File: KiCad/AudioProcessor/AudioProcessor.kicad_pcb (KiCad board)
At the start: 2 copper layers, 56 x 43 mm, 49 parts, among them J1 IN4, J2 IN3, J3 IN2, J4 IN1, J5 AUX, J6 I2C, J7 LOUT, J8 ROUT, J9 POWER, U1 TDA7440

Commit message: Audio processor PCB is ready
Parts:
- removed R4, R5, R6, R7, R8: 600, Resistors_SMD:R_0603
- removed the REF** at (134.0, 71.3)
- removed the REF** at (101.1, 72.1)
- removed the REF** at (101.1, 67.7)
- removed the REF** at (101.0, 63.2)
- removed the REF** at (101.0, 58.6)
- removed the REF** at (118.2, 54.6)
- removed the REF** at (142.6, 90.5)
- removed the REF** at (100.9, 90.6)
- removed the REF** at (135.2, 83.7)
- removed the REF** at (131.2, 83.7)
- removed the REF** at (125.1, 88.1)
- removed the REF** at (121.2, 88.1)
- removed the REF** at (117.4, 88.1)
- removed the REF** at (113.7, 88.1)
- removed the REF** at (105.8, 82.6)
- removed the REF** at (105.8, 78.4)
- added C14: 2uf, Capacitors_SMD:C_0603, F.Cu at (119.5, 86.5)
- added C15: 2uf, Capacitors_SMD:C_0603, F.Cu at (119.5, 89.1)
- added C16: 2uf, Capacitors_SMD:C_0603, F.Cu at (119.5, 91.7)
- added C17: 2uf, Capacitors_SMD:C_0603, F.Cu at (119.5, 94.3)
- added C18: 2uf, Capacitors_SMD:C_0603, F.Cu at (116.2, 87.8)
- added C19: 2uf, Capacitors_SMD:C_0603, F.Cu at (116.2, 90.4)
- added C20: 2uf, Capacitors_SMD:C_0603, F.Cu at (116.3, 93.0)
- added C21: 2uf, Capacitors_SMD:C_0603, F.Cu at (116.3, 95.6)
- added C22: 100uf, Capacitors_THT:CP_Radial_Tantal_D6.0mm_P5.00mm, F.Cu at (141.0, 92.8)
- added C23: 4.7n, Capacitors_THT:C_Rect_L7.0mm_W2.0mm_P5.00mm, F.Cu at (142.1, 105.9)
- added C24: 1n, Capacitors_THT:C_Rect_L7.0mm_W2.0mm_P5.00mm, F.Cu at (142.1, 109.1)
- added J10: DPOT_10K, KiCadCustomLibs:Conn_1x03_2.54mm, F.Cu at (99.6, 89.4)
- added REF**: MountingHole_3mm, Mounting_Holes:MountingHole_3mm, F.Cu at (148.0, 112.0)
- added REF**: MountingHole_3mm, Mounting_Holes:MountingHole_3mm, F.Cu at (100.0, 112.0)
- added REF**: MountingHole_3mm, Mounting_Holes:MountingHole_3mm, F.Cu at (100.0, 83.0)
- added REF**: MountingHole_3mm, Mounting_Holes:MountingHole_3mm, F.Cu at (148.0, 83.0)
- added U2: LM386M, Housings_SOIC:SOIC-8_3.9x4.9mm_Pitch1.27mm, F.Cu at (107.9, 93.1)
- C1: value 2.2uf -> 220uf; footprint Capacitors_THT:C_Rect_L7.0mm_W2.0mm_P5.00mm -> Capacitors_THT:CP_Radial_Tantal_D8.0mm_P5.00mm
- C11: value 5.6n -> 4.7n
- C12: value 5.6n -> 1n
- C13: value 2.2uf -> 10uf; footprint Capacitors_THT:C_Rect_L7.0mm_W2.0mm_P5.00mm -> Capacitors_SMD:C_0603
- C2: value 2.2uf -> 50n; footprint Capacitors_THT:C_Rect_L7.0mm_W2.0mm_P5.00mm -> Capacitors_SMD:C_0603
- C3: value 2.2uf -> 100uf; footprint Capacitors_THT:C_Rect_L7.0mm_W2.0mm_P5.00mm -> Capacitors_THT:CP_Radial_Tantal_D6.0mm_P5.00mm
- C4: value 2.2uf -> 10uf; footprint Capacitors_THT:C_Rect_L7.0mm_W2.0mm_P5.00mm -> Capacitors_THT:CP_Radial_Tantal_D4.5mm_P2.50mm
- C6, C7: value 2.2uf -> 2uf; footprint Capacitors_THT:C_Rect_L7.0mm_W2.0mm_P5.00mm -> Capacitors_SMD:C_0603
- J1, J2, J3, J4, J7, J8, J9: footprint KiCadCustomLibs:Conn2pin_2.54mm -> KiCadCustomLibs:Conn_1x02_2.54mm
- J5: value AUX -> PHONES; footprint Pin_Headers:Pin_Header_Straight_1x03_Pitch2.54mm -> KiCadCustomLibs:Conn_1x02_2.54mm
- J6: footprint Pin_Headers:Pin_Header_Straight_1x03_Pitch2.54mm -> KiCadCustomLibs:Conn_1x03_2.54mm
- R1: value 600 -> 10
- R2, R3: value 600 -> 47K
- moved C4 43.7 mm to (117.4, 104.6)
- moved C3 40.9 mm to (105.5, 99.5), turned to 0 degrees
- moved R2 39.7 mm to (116.5, 97.9)
- moved R3 39.4 mm to (116.5, 99.8)
- moved J3 35.9 mm to (118.9, 82.1), turned to 90 degrees
- moved C1 33.8 mm to (108.9, 105.5), turned to 270 degrees
- moved R1 32.5 mm to (109.0, 89.1), turned to 0 degrees
- moved J1 32.2 mm to (125.5, 82.1), turned to 90 degrees
- moved J6 25.8 mm to (148.1, 102.9), turned to 180 degrees
- moved J7 25.4 mm to (136.0, 82.1)
- moved U1 24.2 mm to (128.6, 96.2)
- moved C5 23.8 mm to (122.4, 112.8)
- moved C8 23.8 mm to (126.0, 107.8)
- moved C9 23.7 mm to (129.6, 112.8)
- moved R10 23.7 mm to (137.5, 112.8)
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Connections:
- C1 pad 2: /IN4 -> Net-(C1-Pad2)
- C12 pad 2: Net-(C12-Pad2) -> Net-(C11-Pad2)
- C2 pad 2: /IN3 -> Net-(C1-Pad1)
- C3 pad 1: Net-(C3-Pad1) -> +9V
- C3 pad 2: /IN2 -> GNDA
- C4 pad 2: /IN1 -> /AUX
- J1 pad 1: /IN4 -> GNDA
- J1 pad 2: GNDA -> /IN4
- J2 pad 1: /IN3 -> GNDA
- J2 pad 2: GNDA -> /IN3
- J3 pad 1: /IN2 -> GNDA
- J3 pad 2: GNDA -> /IN2
- J4 pad 1: /IN1 -> GNDA
- J4 pad 2: GNDA -> /IN1
- J5 pad 1: Net-(C7-Pad2) -> GNDA
- J5 pad 2: GNDA -> Net-(C1-Pad2)
- J6 pad 1: /SDA -> /GND
- J6 pad 3: GND -> /SDA
- J7 pad 1: /LOUT -> GNDA
- J7 pad 2: GNDA -> /LOUT
- J8 pad 1: /ROUT -> GNDA
- J8 pad 2: GNDA -> /ROUT
- J9 pad 1: +9V -> GNDA
- J9 pad 2: GNDA -> +9V
- R1 pad 1: Net-(R1-Pad1) -> Net-(C2-Pad1)
- R1 pad 2: Net-(C1-Pad1) -> GNDA
- R2 pad 1: Net-(R2-Pad1) -> Net-(C6-Pad2)
- R2 pad 2: Net-(C2-Pad1) -> Net-(C4-Pad1)
- R3 pad 1: Net-(R3-Pad1) -> Net-(C7-Pad2)
- R3 pad 2: Net-(C3-Pad1) -> Net-(C4-Pad1)
- U1 pad 1: Net-(R2-Pad1) -> Net-(C18-Pad1)
- U1 pad 18: Net-(C12-Pad2) -> Net-(C23-Pad2)
- U1 pad 2: Net-(R3-Pad1) -> Net-(C15-Pad1)
- U1 pad 20: GND -> /GND
- U1 pad 28: Net-(R1-Pad1) -> Net-(C14-Pad1)
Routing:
- net +9V: track 16.0 -> 58.5 mm, vias 0 -> 2
- net Net-(C2-Pad1): track 30.5 -> 1.55 mm, vias 2 -> 0
- net /AUX: track 0.00 -> 26.6 mm
- net Net-(C7-Pad2): track 30.8 -> 6.82 mm
- net Net-(C6-Pad2): track 29.2 -> 7.28 mm
- net GNDA: track 51.1 -> 30.5 mm, vias 2 -> 6
- net GND: track 19.6 -> 0.00 mm
- net /GND: track 0.00 -> 19.4 mm
- net Net-(R1-Pad1): track 18.9 -> 0.00 mm
- net /IN4: track 9.16 -> 27.4 mm, vias 0 -> 3
- net Net-(C3-Pad1): track 16.8 -> 0.00 mm, vias 2 -> 0
- net Net-(C14-Pad1): track 0.00 -> 14.2 mm
- net Net-(C1-Pad2): track 0.00 -> 13.5 mm
- net /IN3: track 7.03 -> 20.5 mm, vias 0 -> 2
- net /IN2: track 7.75 -> 21.1 mm, vias 0 -> 2
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- added copper zone on F.Cu, net GNDA
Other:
- board size 56 x 43 mm -> 54 x 35 mm
- net class Default: via_dia 2 -> 1.2; via_drill 0.8 -> 0.6
- net class PWR added: clearance 0.3, trace_width 0.8, via_dia 1.3, via_drill 0.6
- board text added: "+"
- board text added: "-"
- board text added: "9V"
- board text added: "GND"
- board text added: "NPPC 2019"
- board text added: "SCL"
- board text added: "SDA"
- board text added: "TDA7440 Audio Processor"

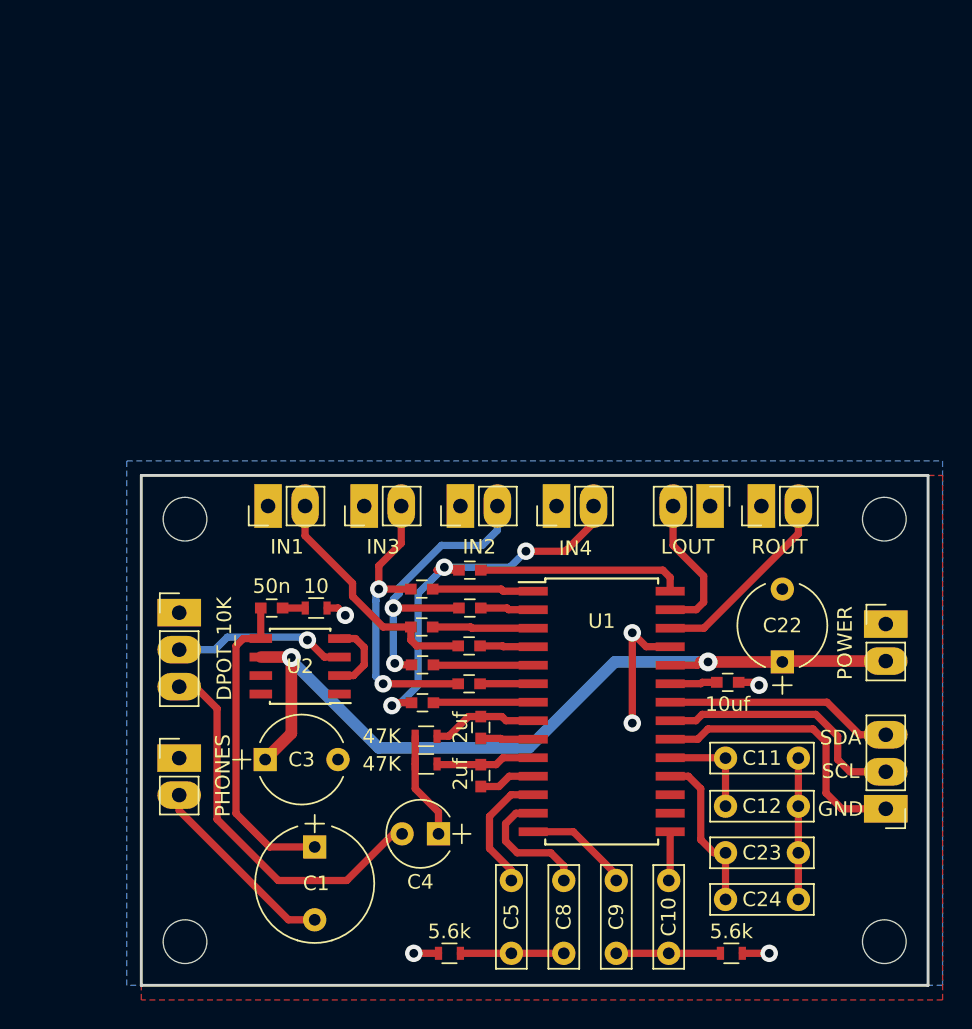
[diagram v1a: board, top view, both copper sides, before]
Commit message: Adjust components according to availability
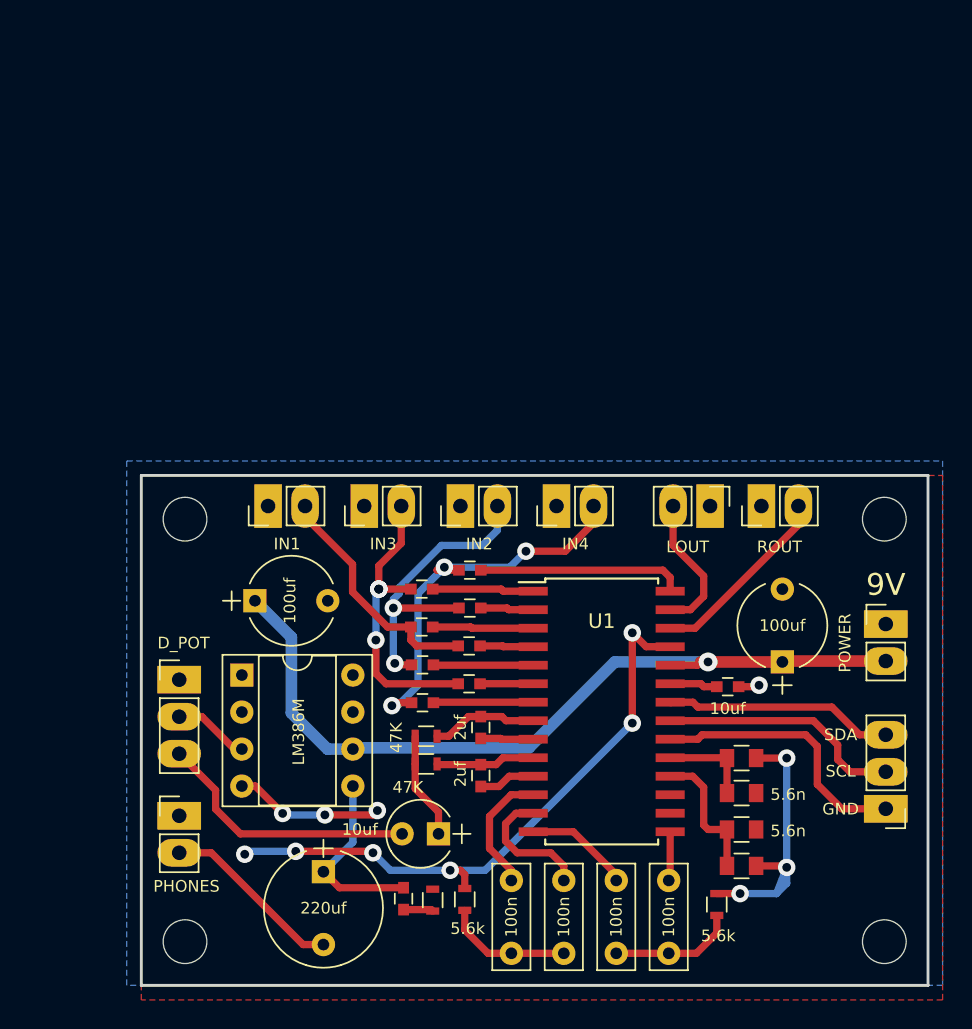
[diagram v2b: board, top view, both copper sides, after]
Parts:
- C10, C5, C8, C9: footprint Capacitors_THT:C_Rect_L7.0mm_W2.0mm_P5.00mm -> Capacitors_THT:C_Rect_L7.2mm_W2.5mm_P5.00mm_FKS2_FKP2_MKS2_MKP2
- C11, C12, C23, C24: footprint Capacitors_THT:C_Rect_L7.0mm_W2.0mm_P5.00mm -> Capacitors_SMD:C_0805
- J10: value DPOT_10K -> D_POT
- U2: footprint Housings_SOIC:SOIC-8_3.9x4.9mm_Pitch1.27mm -> Housings_DIP:DIP-8_W7.62mm_Socket
- moved C2 21.9 mm to (115.0, 109.0), turned to 90 degrees
- moved R1 21.6 mm to (117.0, 109.2), turned to 90 degrees
- moved C3 10.9 mm to (104.8, 88.6)
- moved J10 4.60 mm to (99.6, 94.0)
- moved C24 4.53 mm to (138.2, 106.8)
- moved C23 4.22 mm to (138.2, 104.3)
- moved U2 4.04 mm to (103.9, 93.7), turned to 0 degrees
- moved C12 4.00 mm to (138.2, 101.8)
- moved J5 3.96 mm to (99.6, 103.4)
- moved C11 3.90 mm to (138.2, 99.4)
- moved R9 3.85 mm to (119.2, 109.1), turned to 90 degrees
- moved R10 3.50 mm to (136.5, 109.5), turned to 90 degrees
- moved C1 1.80 mm to (109.5, 107.2)
- moved C13 0.30 mm to (137.2, 94.5)
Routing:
- net GNDA: track 30.5 -> 73.9 mm, vias 6 -> 13
- net Net-(C1-Pad1): track 21.8 -> 12.7 mm
- net /AUX: track 26.6 -> 18.3 mm
- net Net-(J10-Pad2): track 11.9 -> 5.22 mm, vias 1 -> 0
- net +9V: track 58.5 -> 55.8 mm, vias 2 -> 1
- net Net-(C23-Pad2): track 11.2 -> 9.44 mm
- net Net-(C5-Pad1): track 7.10 -> 8.81 mm
- net Net-(C10-Pad2): track 7.15 -> 8.68 mm
- net Net-(C1-Pad2): track 13.5 -> 12.5 mm
- net /GND: track 19.4 -> 18.6 mm
- net Net-(C11-Pad2): track 7.11 -> 6.31 mm
- net /SCL: track 17.5 -> 16.8 mm
- net /IN3: track 20.5 -> 20.4 mm, vias 2 -> 3
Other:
- rule pad_to_mask_clearance: 0.2 -> 0.1
- board text added: "5.6n"
